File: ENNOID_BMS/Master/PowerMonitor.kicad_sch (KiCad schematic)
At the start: 103 parts, among them J15 Charge +, U1 AMC1301 or AMC1302, U10 SN6501DBV, U12 AMC1301, U13 AMC1301, U15A OPA2197IDR, U15B OPA2197IDR, U15C OPA2197IDR, U16 ISL28022, U3 TPS76350, U4 SN6501DBV, U5 SFH617A-2X009T, U6 TPS76350

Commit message: ENNOID BMS PCBs completed
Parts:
- removed U15A, U15B, U15C: OPA2197IDR, Housings_SOIC:SOIC-8_3.9x4.9mm_Pitch1.27mm, symbol Amplifier_Operational:OPA2376xxD
- added U14: OPA2197IDR, Package_SO:SOIC-8_3.9x4.9mm_P1.27mm, symbol Amplifier_Operational:OPA2197xD
- D14, D15, D17, D18: footprint Diodes_SMD:D_SOD-123 -> Diode_SMD:D_SOD-123
- U1, U12, U13: footprint Housings_SOIC:SSO-8_6.8x5.9mm_Pitch1.27mm_Clearance8mm -> ENNOID:SSO-8_6.8x5.9mm_Pitch1.27mm_Clearance8mm
- U16: footprint Housings_SSOP:MSOP-10_3x3mm_Pitch0.5mm -> Package_SO:MSOP-10_3x3mm_P0.5mm
- U5: footprint Housings_DIP:SMDIP-4_W9.53mm_Clearance8mm -> Package_DIP:SMDIP-4_W9.53mm_Clearance8mm
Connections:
- net +12V: now also U14.8 (V+)
- net GND: now also U14.4 (V-)
- net Vbat: now also U14.1
- net at R156.2, R160.1: now also U14.3 (+)
- net at R155.2, R164.1: now also U14.2 (-)
- net at R157.2, R165.1: now also U14.6 (-)
- net at R158.2, R161.1: now also U14.5 (+)
- net at R16.1, R165.2: now also U14.7

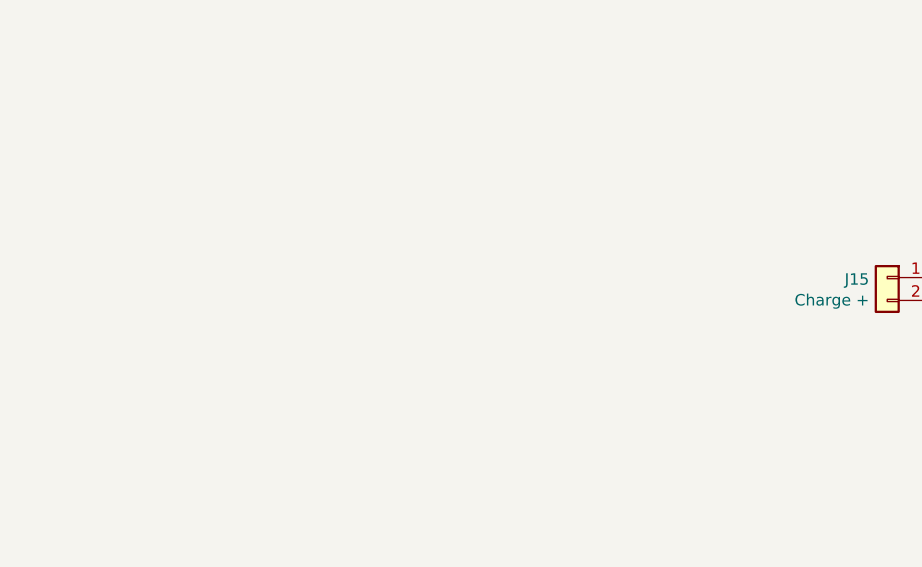
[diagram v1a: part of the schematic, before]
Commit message: bms architecture notes made re charging and discharging
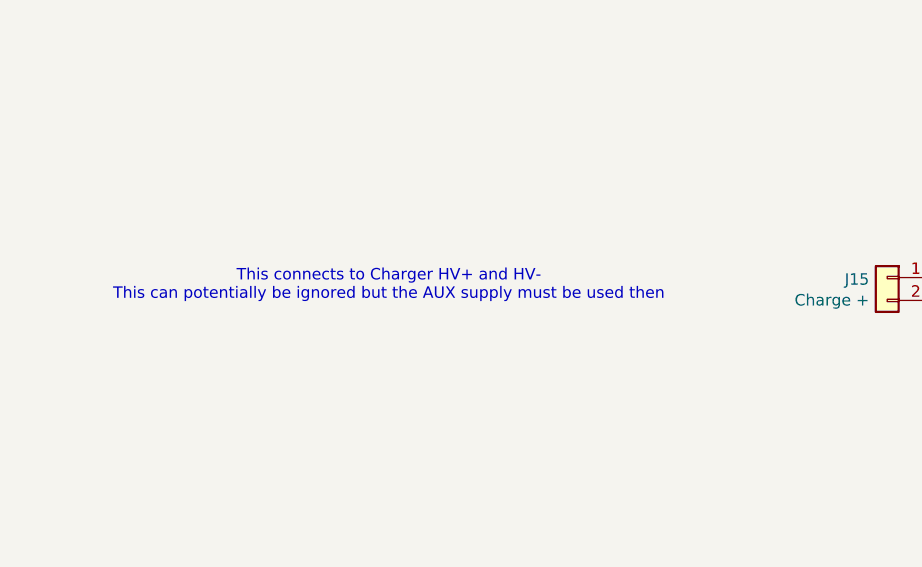
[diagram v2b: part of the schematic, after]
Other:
- note added: "This connects to Charger HV+ and HV- This can potentially be ignored but the AUX supply must be used then"
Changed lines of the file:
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@@
+		)
+	)
+	(text "This connects to Charger HV+ and HV-\nThis can potentially be ignored but the AUX supply must be used then"
+		(exclude_from_sim no)
+		(at 70.358 189.484 0)
+		(effects
+			(font
+				(size 1.27 1.27)
+			)
 		)
 	)

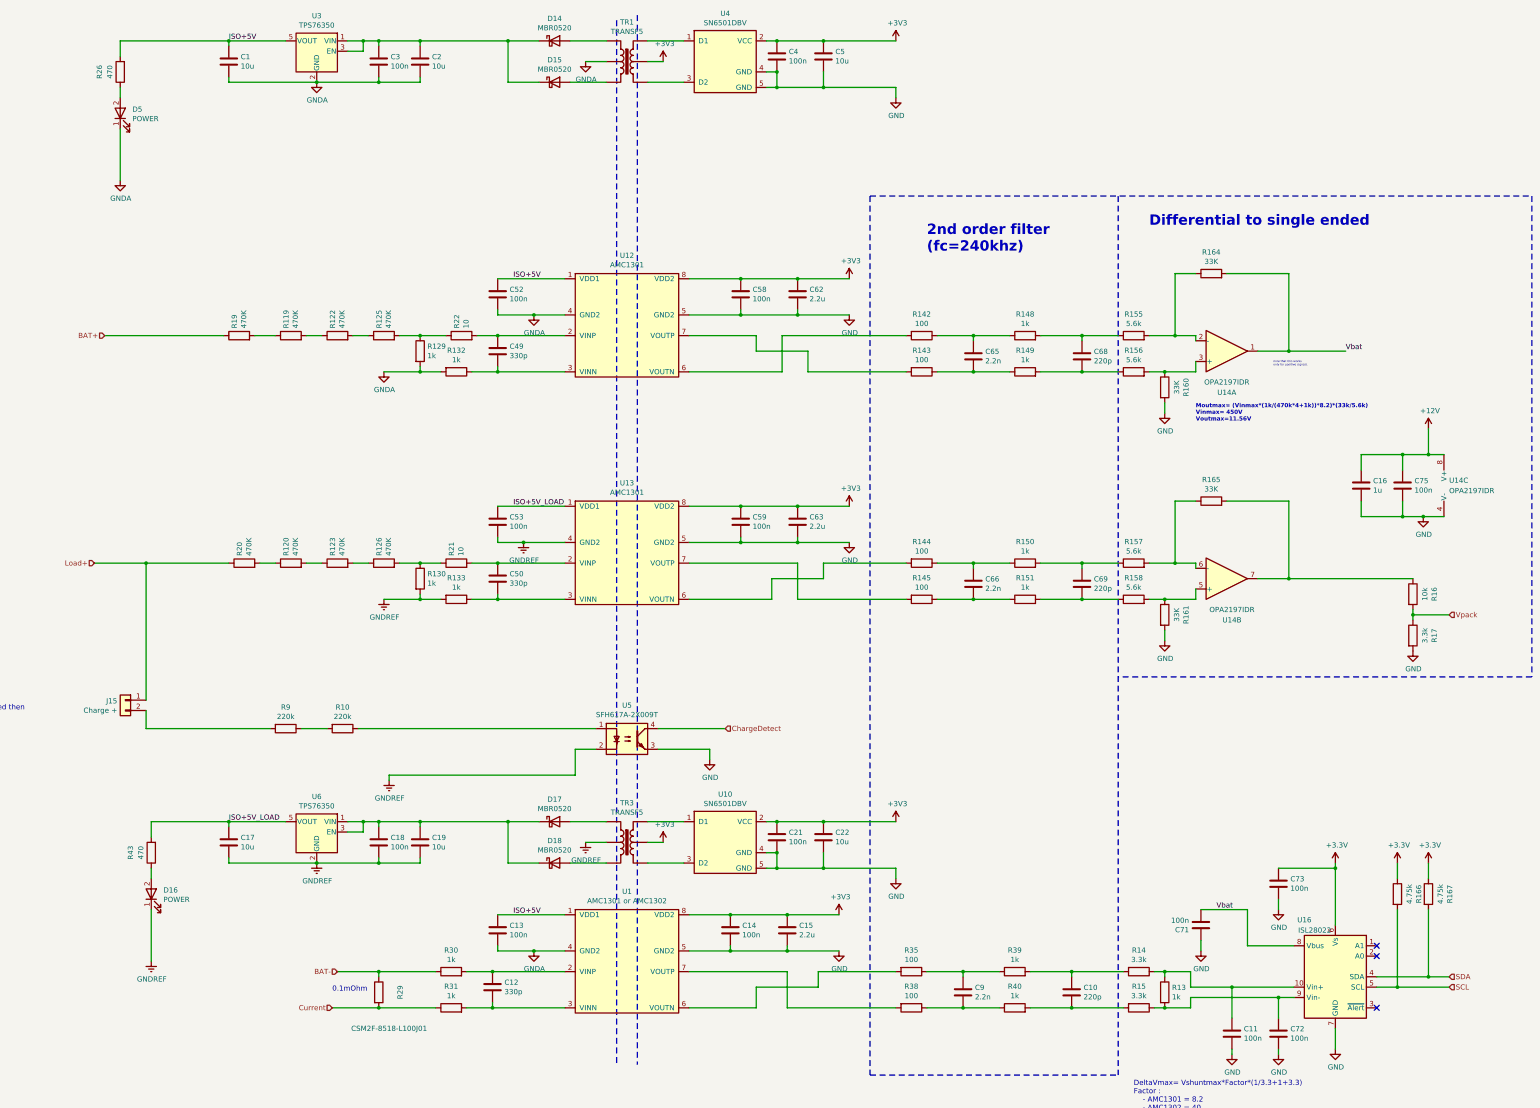
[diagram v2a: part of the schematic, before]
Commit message: Slave with SMD and no other fuses
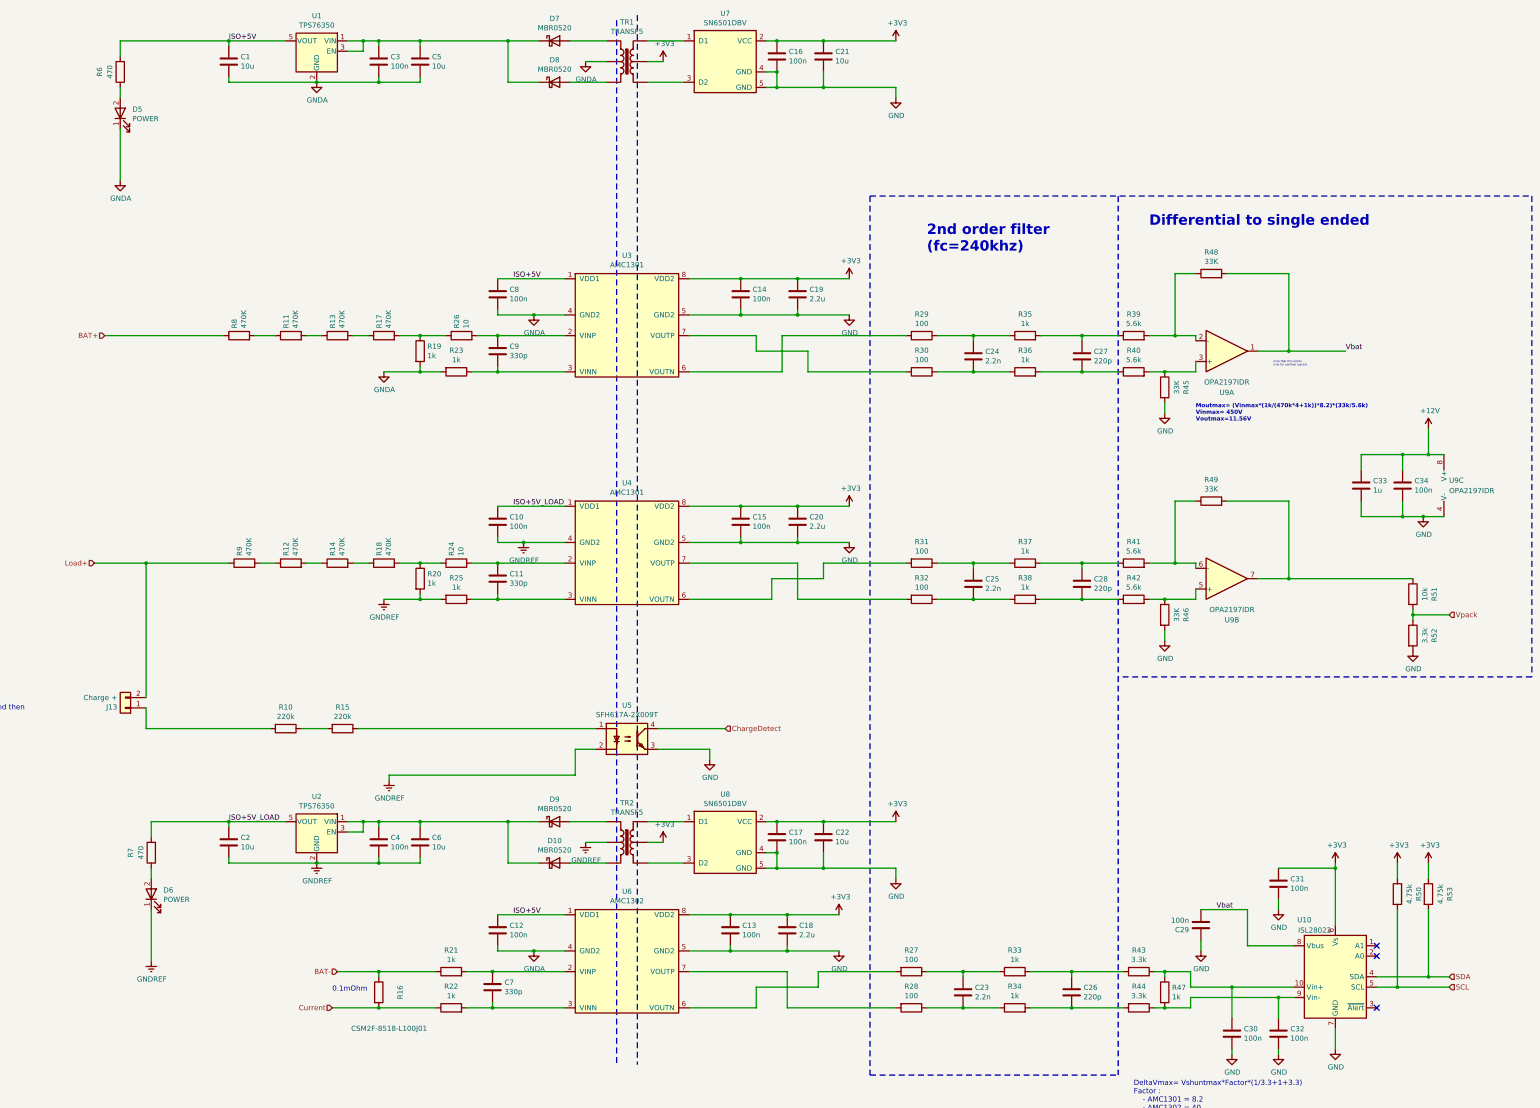
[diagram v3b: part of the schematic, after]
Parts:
- J13: renamed from J15; footprint Connector_Phoenix_GMSTB:PhoenixContact_GMSTBVA_2,5_2-G_1x02_P7.50mm_Vertical -> Kicad_Libraries:Phoenix_1x2_1729128; MPN 30.102 -> 1729128
- U6: renamed from U1; value AMC1301 or AMC1302 -> AMC1302; MPN AMC1301DWV -> AMC1302
- U9: renamed from U14; MPN (none) -> OPA2197IDR
- renumbered C53 to C10, C50 to C11, C13 to C12, C14 to C13, C58 to C14, C59 to C15, C4 to C16, C21 to C17, C15 to C18, C62 to C19, C17 to C2, C63 to C20, C5 to C21, C9 to C23, C65 to C24, C66 to C25, C10 to C26, C68 to C27, C69 to C28, C71 to C29, C11 to C30, C73 to C31, C72 to C32, C16 to C33, C75 to C34, C18 to C4, C2 to C5, C19 to C6, C12 to C7, C52 to C8, C49 to C9, D18 to D10, D16 to D6, D14 to D7, D15 to D8, D17 to D9, R9 to R10, R119 to R11, R120 to R12, R122 to R13, R123 to R14, R10 to R15, R29 to R16, R125 to R17, R126 to R18, R129 to R19, R130 to R20, R30 to R21, R31 to R22, R132 to R23, R21 to R24, R133 to R25, R22 to R26, R35 to R27, R38 to R28, R142 to R29, R143 to R30, R144 to R31, R145 to R32, R39 to R33, R40 to R34, R148 to R35, R149 to R36, R150 to R37, R151 to R38, R155 to R39, R156 to R40, R157 to R41, R158 to R42, R14 to R43, R15 to R44, R160 to R45, R161 to R46, R13 to R47, R164 to R48, R165 to R49, R166 to R50, R16 to R51, R17 to R52, R167 to R53, R26 to R6, R43 to R7, R19 to R8, R20 to R9, TR3 to TR2, U3 to U1, U16 to U10, U6 to U2, U12 to U3, U13 to U4, U4 to U7, U10 to U8
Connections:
- net +3.3V is gone; now on net +3V3: C31.2, R50.1, R53.1, U10.6 (Vs)
- net Load+: now also J13.2 (Pin_2); no longer J13.1 (Pin_1)
- net at R10.2: now also J13.1 (Pin_1); no longer J13.2 (Pin_2)
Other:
- moved on the sheet: J13

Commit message: fuse boards
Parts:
- R10, R15: MPN 25121WF2203T4E -> CRCW2512220KFKEG
- R19, R20, R21, R22, R23, R25, R33, R34, R35, R36, R37, R38, R47: MPN MCR03EZPFX1001 -> MCWR06X1001FTL
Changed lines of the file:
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@@
 			)
 		)
-		(property "Datasheet" "https://docs.rs-online.com/50c7/0900766b814716fc.pdf"
+		(property "Datasheet" "https://www.farnell.com/datasheets/1849611.pdf?_ga=1.99182808.792448772.1482467944"
 			(at 198.12 158.75 0)
 			(effects
@@
 			)
 		)
-		(property "MPN" "MCR03EZPFX1001"
+		(property "MPN" "MCWR06X1001FTL"
 			(at 198.12 158.75 0)
 			(effects
@@
 			)
 		)
-		(property "Datasheet" "https://docs.rs-online.com/50c7/0900766b814716fc.pdf"
+		(property "Datasheet" "https://www.farnell.com/datasheets/1849611.pdf?_ga=1.99182808.792448772.1482467944"
 			(at 207.01 163.83 0)
 			(effects
@@
 			)
 		)
-		(property "MPN" "MCR03EZPFX1001"
+		(property "MPN" "MCWR06X1001FTL"
 			(at 207.01 163.83 0)
 			(effects
@@
 			)
 		)
-		(property "Datasheet" "https://docs.rs-online.com/50c7/0900766b814716fc.pdf"
+		(property "Datasheet" "https://www.farnell.com/datasheets/1849611.pdf?_ga=1.99182808.792448772.1482467944"
 			(at 346.71 154.94 0)
 			(effects
@@
 			)
 		)
-		(property "MPN" "MCR03EZPFX1001"
+		(property "MPN" "MCWR06X1001FTL"
 			(at 346.71 154.94 0)
 			(effects
@@
 			)
 		)
-		(property "Datasheet" "https://docs.rs-online.com/50c7/0900766b814716fc.pdf"
+		(property "Datasheet" "https://www.farnell.com/datasheets/1849611.pdf?_ga=1.99182808.792448772.1482467944"
 			(at 346.71 163.83 0)
 			(effects
@@
 			)
 		)
-		(property "MPN" "MCR03EZPFX1001"
+		(property "MPN" "MCWR06X1001FTL"
 			(at 346.71 163.83 0)
 			(effects
@@
 			)
 		)
-		(property "Datasheet" "https://docs.rs-online.com/50c7/0900766b814716fc.pdf"
+		(property "Datasheet" "https://www.farnell.com/datasheets/1849611.pdf?_ga=1.99182808.792448772.1482467944"
 			(at 198.12 102.87 0)
 			(effects
@@
 			)
 		)
-		(property "MPN" "MCR03EZPFX1001"
+		(property "MPN" "MCWR06X1001FTL"
 			(at 198.12 102.87 0)
 			(effects
@@
 			)
 		)
-		(property "Datasheet" "https://docs.rs-online.com/50c7/0900766b814716fc.pdf"
+		(property "Datasheet" "https://www.farnell.com/datasheets/1849611.pdf?_ga=1.99182808.792448772.1482467944"
 			(at 207.01 107.95 0)
 			(effects
@@
 			)
 		)
-		(property "MPN" "MCR03EZPFX1001"
+		(property "MPN" "MCWR06X1001FTL"
 			(at 207.01 107.95 0)
 			(effects
@@
 			)
 		)
-		(property "Datasheet" "https://docs.rs-online.com/50c7/0900766b814716fc.pdf"
+		(property "Datasheet" "https://www.farnell.com/datasheets/1849611.pdf?_ga=1.99182808.792448772.1482467944"
 			(at 346.71 99.06 0)
 			(effects
@@
 			)
 		)
-		(property "MPN" "MCR03EZPFX1001"
+		(property "MPN" "MCWR06X1001FTL"
 			(at 346.71 99.06 0)
 			(effects
@@
 			)
 		)
-		(property "Datasheet" "https://docs.rs-online.com/50c7/0900766b814716fc.pdf"
+		(property "Datasheet" "https://www.farnell.com/datasheets/1849611.pdf?_ga=1.99182808.792448772.1482467944"
 			(at 346.71 107.95 0)
 			(effects
@@
 			)
 		)
-		(property "MPN" "MCR03EZPFX1001"
+		(property "MPN" "MCWR06X1001FTL"
 			(at 346.71 107.95 0)
 			(effects
@@
 			)
 		)
-		(property "Datasheet" "https://www.royalohm.com/assets/pdf/products/smd/1.pdf"
+		(property "Datasheet" "https://www.vishay.com/docs/20035/dcrcwe3.pdf"
 			(at 179.07 195.58 0)
 			(effects
@@
 			)
 		)
-		(property "MPN" "25121WF2203T4E"
+		(property "MPN" "CRCW2512220KFKEG"
 			(at 179.07 195.58 0)
 			(effects
@@
 			)
 		)
-		(property "Datasheet" "https://www.royalohm.com/assets/pdf/products/smd/1.pdf"
+		(property "Datasheet" "https://www.vishay.com/docs/20035/dcrcwe3.pdf"
 			(at 165.1 195.58 0)
 			(effects
@@
 			)
 		)
-		(property "MPN" "25121WF2203T4E"
+		(property "MPN" "CRCW2512220KFKEG"
 			(at 165.1 195.58 0)
 			(effects
@@
 			)
 		)
-		(property "Datasheet" "https://docs.rs-online.com/50c7/0900766b814716fc.pdf"
+		(property "Datasheet" "https://www.farnell.com/datasheets/1849611.pdf?_ga=1.99182808.792448772.1482467944"
 			(at 381 260.35 0)
 			(effects
@@
 			)
 		)
-		(property "MPN" "MCR03EZPFX1001"
+		(property "MPN" "MCWR06X1001FTL"
 			(at 381 260.35 0)
 			(effects
@@
 			)
 		)
-		(property "Datasheet" "https://docs.rs-online.com/50c7/0900766b814716fc.pdf"
+		(property "Datasheet" "https://www.farnell.com/datasheets/1849611.pdf?_ga=1.99182808.792448772.1482467944"
 			(at 205.74 255.27 0)
 			(effects
@@
 			)
 		)
-		(property "MPN" "MCR03EZPFX1001"
+		(property "MPN" "MCWR06X1001FTL"
 			(at 205.74 255.27 0)
 			(effects
@@
 			)
 		)
-		(property "Datasheet" "https://docs.rs-online.com/50c7/0900766b814716fc.pdf"
+		(property "Datasheet" "https://www.farnell.com/datasheets/1849611.pdf?_ga=1.99182808.792448772.1482467944"
 			(at 205.74 264.16 0)
 			(effects
@@
 			)
 		)
-		(property "MPN" "MCR03EZPFX1001"
+		(property "MPN" "MCWR06X1001FTL"
 			(at 205.74 264.16 0)
 			(effects
@@
 			)
 		)
-		(property "Datasheet" "https://docs.rs-online.com/50c7/0900766b814716fc.pdf"
+		(property "Datasheet" "https://www.farnell.com/datasheets/1849611.pdf?_ga=1.99182808.792448772.1482467944"
 			(at 344.17 255.27 0)
 			(effects
@@
 			)
 		)
-		(property "MPN" "MCR03EZPFX1001"
+		(property "MPN" "MCWR06X1001FTL"
 			(at 344.17 255.27 0)
 			(effects
@@
 			)
 		)
-		(property "Datasheet" "https://docs.rs-online.com/50c7/0900766b814716fc.pdf"
+		(property "Datasheet" "https://www.farnell.com/datasheets/1849611.pdf?_ga=1.99182808.792448772.1482467944"
 			(at 344.17 264.16 0)
 			(effects
@@
 			)
 		)
-		(property "MPN" "MCR03EZPFX1001"
+		(property "MPN" "MCWR06X1001FTL"
 			(at 344.17 264.16 0)
 			(effects
